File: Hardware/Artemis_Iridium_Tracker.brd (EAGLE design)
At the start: 50.8 x 50.8 mm, 160 parts, among them J1 IRIDIUM_9603N, J14 CORTEX_DEBUG, J3 PTH, J8 uFL, J9 SMA-142-0711-821/826, Q1 DMG3414U-7, Q2 DMG3415U-7, U10 MCP73831, U2 LTC3225EDDB#TRMPBF, U3 ADM4210-1, U4 UBLOX_ZOE_M8-0-10, U5 AS179-92LF, U6 MS8607-02BA01, U7 ARTEMIS_MODULESMD, U8 AP3429A, U9 CH340E, Y1 32.768kHz, Y2 32.768kHz

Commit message: Updated the PCB - still work in progress!
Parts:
- removed BYP: (no value), SparkFun-Jumpers:SMT-JUMPER_2_NO_SILK
- removed C32: 0.1uF, SparkFun-Capacitors:0603
- removed C33: 1nF, SparkFun-Capacitors:0603
- removed C34, C35: 4.7uF, SparkFun-Capacitors:0603
- removed D15: 3A/10V/280mV, SparkFun-DiscreteSemi:SOD-323
- removed F1: 6V/2A, SparkFun-Fuses:1210
- removed J10: (no value), SparkFun-Connectors:USB-C-16P
- removed J11: (no value), SparkFun-Connectors:1X05
- removed J12: (no value), SparkFun-Connectors:JST-2-SMD
- removed J14: CORTEX_DEBUG, SparkFun-Connectors:2X5-PTH-1.27MM-NO_SILK
- removed J16: (no value), SparkFun-Connectors:JST04_1MM_RA
- removed J8: uFL, microbuilder:U.FL
- removed J9: SMA-142-0711-821/826, con-coax:J502-ND-142-0711-821/826
- removed JP3: JUMPER-SMT_2_NC_TRACE_SILK, SparkFun-Jumpers:SMT-JUMPER_2_NC_TRACE_SILK
- removed L3: 2.2μH, SparkFun-Coils:INDUCTOR_4X4MM
- removed LOGO1: OSHW-LOGOMINI, SparkFun-Aesthetics:OSHW-LOGO-MINI
- removed LOGO2: SFE_LOGO_NAME.1_INCH, SparkFun-Aesthetics:SFE_LOGO_NAME_.1
- removed LOGO3: SFE_LOGO_NAME_FLAME.1_INCH, SparkFun-Aesthetics:SFE_LOGO_NAME_FLAME_.1
- removed S2: RESET, SparkFun-Switches:TACTILE_SWITCH_SMD_5.2MM
- removed U10: MCP73831, SparkFun-IC-Power:SOT23-5
- removed Y1, Y2: 32.768kHz, SparkFun-Clocks:CRYSTAL-SMD-3.2X1.5MM
- added !RESET, EN, GND: (no value), SparkFun-Connectors:1X01_NO_SILK
- added 3V3EN: (no value), SparkFun-Jumpers:SMT-JUMPER_2_NC_TRACE_SILK
- added 5V3, BUSV, RX(OUT), RX0, TX(IN), TX0: TEST-POINT3X5, SparkFun-Connectors:PAD.03X.05
- added C1: 10nF, SparkFun-Capacitors:0603
- added C7: 0.1uF, SparkFun-Capacitors:0603
- added C8: 4.7uF, SparkFun-Capacitors:0603
- added D13: Yellow, SparkFun-LED:LED-0603
- added DEBUG: CORTEX_DEBUG, SparkFun-Connectors:2X5-PTH-1.27MM-NO_SILK
- added I2C: PTH, SparkX:1X04_NO_SILK
- added JP2: JUMPER-SMT_2_NC_TRACE_SILK, SparkFun-Jumpers:SMT-JUMPER_2_NC_TRACE_SILK
- added L2: 2.2μH, SparkFun-Coils:INDUCTOR_4X4MM
- added LOGO4: OSHW-LOGOMINI, SparkFun-Aesthetics:OSHW-LOGO-MINI
- added Q3: DMG3415U-7, microbuilder:SOT23-WIDE
- added Q4: 2N2222, transistor:SOT23-BEC
- added QWIIC: (no value), SparkFun-Connectors:JST04_1MM_RA
- added R2, R3: 1k, SparkFun-Resistors:0603
- added R20, R4: 5.1k, SparkFun-Resistors:0603
- added R30: 10k, SparkFun-Resistors:0603
- added S1: RESET, SparkFun-Switches:TACTILE_SWITCH_SMD_5.2MM
- added SPI: (no value), SparkFun-Connectors:1X07
- added U$29, U$30: SPARKX-LOGO4, SparkX:SPARKX-MEDIUM
- added U$31: (no value), SCK_BOT:SCK0
- added U$32: (no value), 5.3V:5#3V0
- added U$33: (no value), RX:RX0
- added U$34: (no value), RX0:RX00
- added U$35: (no value), RX1:RX10
- added U$36: (no value), SAFEBOOT:SAFEBOOT0
- added U$37: (no value), TX:TX0
- added U$38: (no value), TX0:TX00
- added U$39: (no value), TX1:TX10
- added U$40: (no value), ARTEMIS:ARTEMIS0
- added U$41: (no value), IRIDIUM:IRIDIUM0
- added U$42: (no value), TRACKER:TRACKER0
- added U$43: (no value), PWR_LED:PWR_LED0
- added U$44: (no value), VBUS:VBUS0
- added U$45: (no value), GND:GND0
- added U$46: (no value), EN:EN0
- added U$47: (no value), 3.3V EN:3#3V_EN0
- added U$48: (no value), MEAS:MEAS0
- added U$49: (no value), LiPo:LIPO0
- added U1: CH340E_MSOP10, SparkFun-IC-Comms:MSOP10
- added X1, X2: 32.768kHz, SparkFun-Clocks:CRYSTAL-SMD-3.2X1.5MM
- BAT1, BAT2, BAT3: device SparkFun-Electromechanical:BATTERY-AAA-KEYSTONE92 -> Iridium_9603_Beacon:BATTERY-AAA-KEYSTONE82
- C17: value 1.0uF -> 4.7uF
- C29: value 10nF -> 1nF
- D7: value Yellow -> GREEN
- D8: value GREEN -> 3A/10V/280mV; device SparkFun-LED:LED-0603 -> SparkFun-DiscreteSemi:SOD-323
- J2: value (none) -> USB-C; device SparkFun-Connectors:1X02_NO_SILK -> SparkFun-Connectors:USB-C-16P
- J3: value PTH -> (none); device SparkX:1X04_NO_SILK -> SparkFun-Connectors:JST-2-SMD
- J5: device SparkFun-Connectors:1X01_NO_SILK -> SparkFun-Connectors:JST-2-SMD
- J6: value (none) -> uFL; device SparkFun-Connectors:1X01_NO_SILK -> microbuilder:U.FL
- J7: value (none) -> SMA-142-0711-821/826; device SparkFun-Connectors:1X01_NO_SILK -> con-coax:J502-ND-142-0711-821/826
- R22: value 1k -> 10k
- R23: value 330 -> 10k; device SparkFun-Resistors:0603@2 -> SparkFun-Resistors:0603
- R24: value 5.1k -> 20k; device SparkFun-Resistors:0603@2 -> SparkFun-Resistors:0603
- R25: value 5.1k -> 1k; device SparkFun-Resistors:0603@2 -> SparkFun-Resistors:0603
- U$11: device 5.3V_OUT:5#3V0 -> MISO:MISO0
- U$12, U$17: device Qwiic_007:QWIIC0 -> Labels-0_04:GND1
- U$16, U$7: device Labels:RST#-[> -> RESET:#RESET0
- U$18: device Iridium_007:IRIDIUM0 -> SCK:SCK0
- U$19: device Iridium_007:IRIDIUM0 -> GNSS:GNSS0
- U$20, U$24: device 9603N_007:9603N0 -> Labels-0_04:3#3V2
- U$25: device Qwiic_Bubble:QWIIC0 -> MOSI_BOT:MOSI0
- U$28: device 5.3V_OUT:5#3V0 -> MISO_BOT:MISO0
- U$5: device Labels-0_04:SDA8 -> SCL_BOT:SCL0
- U$6: device Labels-0_04:SCL9 -> SDA_BOT:SDA0
- U$8: device Labels:I_SUPER2_C-()-03 -> MOSI:MOSI0
- U9: value CH340E -> MCP73831; device SparkFun-IC-Comms:MSOP10 -> SparkFun-IC-Power:SOT23-5
- moved D14 158.9 mm to (11.4, 38.1), turned to 180 degrees
- moved BAT1 158.8 mm to (5.08, 38.1), turned to 270 degrees
- moved D10 158.2 mm to (11.4, 40.6), turned to 180 degrees
- moved BAT2 133.6 mm to (31.8, 5.08)
- moved U6 133.2 mm to (8.89, 31.1), turned to 180 degrees
- moved C12 131.4 mm to (11.8, 30.9), turned to 90 degrees
- moved GPS_RX 129.8 mm to (48.3, 50.8)
- moved GPS_TX 129.8 mm to (48.3, 48.3)
- moved SAFEBOOT 125.6 mm to (50.8, 55.9)
- moved D9 115.6 mm to (10.3, 15.2)
- moved U$15 112.1 mm to (11.3, 62.6), flipped to the bottom
- moved R29 111.7 mm to (10.3, 17.4)
- moved R28 110.5 mm to (7.62, 20.7), turned to 90 degrees
- moved D1 110.2 mm to (52.8, 18.0)
- moved D2 110.2 mm to (52.8, 20.5)
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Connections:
- removed net ARTEMIS_SHLD: J10.SHLD1, J10.SHLD2, J10.SHLD3, J10.SHLD4, J10.SHLD5, J10.SHLD6, J10.SHLD7, J10.SHLD8
- removed net CC1: J10.A5, R25.2
- removed net CC2: J10.B5, R24.2
- removed net D+1: J10.A6, J10.B6, U9.1
- removed net D-1: J10.A7, J10.B7, U9.2
- removed net N$38 (its old number): BYP.1, F1.1, J10.VBUS1, J10.VBUS2
- new net CC3: J2.B5, R4.2
- new net CC4: J2.A5, R20.2
- new net D+2: J2.A6, J2.B6, U1.1
- new net D-2: J2.A7, J2.B7, U1.2
- new net N$22: D7.A, R3.1
- new net N$34: D13.A, R2.1
- new net N$46: Q3.3, R24.1
- new net N$47: Q4.B, R25.2
- new net SHLD: J2.SHLD1, J2.SHLD2, J2.SHLD3, J2.SHLD4, J2.SHLD5, J2.SHLD6, J2.SHLD7, J2.SHLD8
- net 3.3V: now also C1.1, C12.1, C7.1, DEBUG.1, I2C.2, JP2.2, L2.P$2, QWIIC.2, R2.2, R3.2, SPI.7, U1.10, U1.7, U6.1; no longer C17.1, C29.1, C30.1, J11.5, J14.1, J16.2, L3.P$2, R1.2, R22.2, R23.2, U9.10, U9.7
- net 3V3SW: no longer C12.1, J3.2, U6.1
- net ANTENNA: now also J7.1; no longer J9.1
- net ARTEMIS_!RESET: now also !RESET.1, C29.1, DEBUG.10, S1.3, S1.4; no longer C33.1, J14.10, J5.1, S2.3, S2.4
- net ARTEMIS_!RTS!: now also C30.1, U1.4; no longer C32.1, U9.4
- net ARTEMIS_BOOT: now also C30.2; no longer C32.2
- net ARTEMIS_D10: now also U4.50; no longer U4.36
- net ARTEMIS_D13: now also BUSV.P$1, R23.1, R24.2
- net ARTEMIS_D24: now also TX(IN).P$1
- net ARTEMIS_D25: now also RX(OUT).P$1
- net ARTEMIS_D33: now also DEBUG.6; no longer J14.6
- net ARTEMIS_D34: now also R25.1, R30.1
- net ARTEMIS_D35: now also SPI.5
- net ARTEMIS_D39_SCL4: now also QWIIC.4; no longer J16.4
- net ARTEMIS_D4: now also SPI.6
- net ARTEMIS_D40_SDA4: now also QWIIC.3; no longer J16.3
- net ARTEMIS_D42: no longer J6.1
- net ARTEMIS_D5_SCK: now also SPI.4; no longer J11.4
- net ARTEMIS_D6_MISO: now also SPI.3; no longer J11.3
- net ARTEMIS_D7_MOSI: now also SPI.2; no longer J11.2
- net ARTEMIS_D8_SCL: now also I2C.4; no longer J3.4
- net ARTEMIS_D9_SDA: now also I2C.3; no longer J3.3
- net ARTEMIS_RX0: now also D13.C, RX0.P$1, U1.8; no longer D7.C, U9.8
- net ARTEMIS_SWDCK: now also DEBUG.4; no longer J14.4
- net ARTEMIS_SWDIO: now also DEBUG.2; no longer J14.2
- net ARTEMIS_TX0: now also D7.C, TX0.P$1, U1.9; no longer D8.C, U9.9
- net EXT_PWR: now also 5V3.P$1; no longer J7.1
- net GND: now also C1.2, C7.2, C8.2, DEBUG.3, DEBUG.5, DEBUG.9, GND.1, I2C.1, J2.GND, J2.GND2, J5.1, J6.1, J6.2, J7.G@1, J7.G@2, J7.G@3, J7.G@4, Q4.E, QWIIC.1, R20.1, R23.2, R30.2, R4.1, S1.1, S1.2, SPI.1, U1.3, U9.2; no longer C30.2, C33.2, C34.2, C35.2, J10.GND, J10.GND2, J11.1, J12.1, J14.3, J14.5, J14.9, J16.1, J2.1, J8.1, J8.2, J9.G@1, J9.G@2, J9.G@3, J9.G@4, R24.1, R25.1, S2.1, S2.2, U10.2, U9.3
- net IRIDIUM: now also J6.3; no longer J8.3
- net N$18: now also X2.P$2; no longer Y1.P$2
- net N$19: now also X2.P$1; no longer Y1.P$1
- net N$23: now also D1.A; no longer JP3.2
- net N$3: now also JP2.1, R1.2; no longer D1.A, JP3.1
- net N$31: now also X1.P$1; no longer Y2.P$1
- net N$33: now also L2.P$1; no longer L3.P$1
- net N$36: now also 3V3EN.2, EN.1, U8.1; no longer D8.A, R23.1
- net N$37: now also Q3.1, Q4.C; no longer D7.A
- net N$39: now also U9.5; no longer U10.5
- net N$41: now also U9.1; no longer U10.1
- net N$42: now also J3.2
- net N$45: now also D8.C; no longer D15.C
- net N$7: now also X1.P$2; no longer Y2.P$2
- net VIN: now also 3V3EN.1, Q3.2, R22.2; no longer U8.1
- net V_BATT: now also C8.1, D8.A, J5.2, U9.3; no longer C35.1, D15.A, J12.2, J2.2, U10.3
- net V_USB: now also C17.1, J2.VBUS1, J2.VBUS2, U9.4; no longer BYP.2, C34.1, F1.2, U10.4
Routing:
- net GND: track 54.0 -> 185.8 mm, vias 11 -> 45
- net N$42: track 0.00 -> 115.9 mm, vias 0 -> 2
- net V_USB: track 0.00 -> 64.3 mm, vias 0 -> 2
- net N$24: track 0.00 -> 53.7 mm, vias 0 -> 2
- net 3.3V: track 0.00 -> 44.1 mm, vias 0 -> 1
- net V_BATT: track 0.00 -> 39.0 mm, vias 0 -> 2
- net ARTEMIS_BOOT: track 0.00 -> 31.6 mm, vias 0 -> 4
- net N$43: track 0.00 -> 30.8 mm
- net N$38: track 0.00 -> 30.8 mm
- net N$1: track 18.2 -> 45.4 mm, vias 0 -> 1
- net LTC3225_VOUT: track 22.1 -> 48.6 mm
- net ARTEMIS_!RESET: track 0.00 -> 25.3 mm
- net VIN: track 0.00 -> 24.4 mm, vias 0 -> 1
- net ARTEMIS_D9_SDA: track 0.00 -> 16.9 mm, vias 0 -> 1
- net ARTEMIS_D8_SCL: track 0.00 -> 16.2 mm, vias 0 -> 1
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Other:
- board size 50.8 x 50.8 mm -> 63.5 x 69.8 mm
- board text added: "To Do: Check the height clearance for L2"
- board text removed: "RX"
- board text removed: "TX"

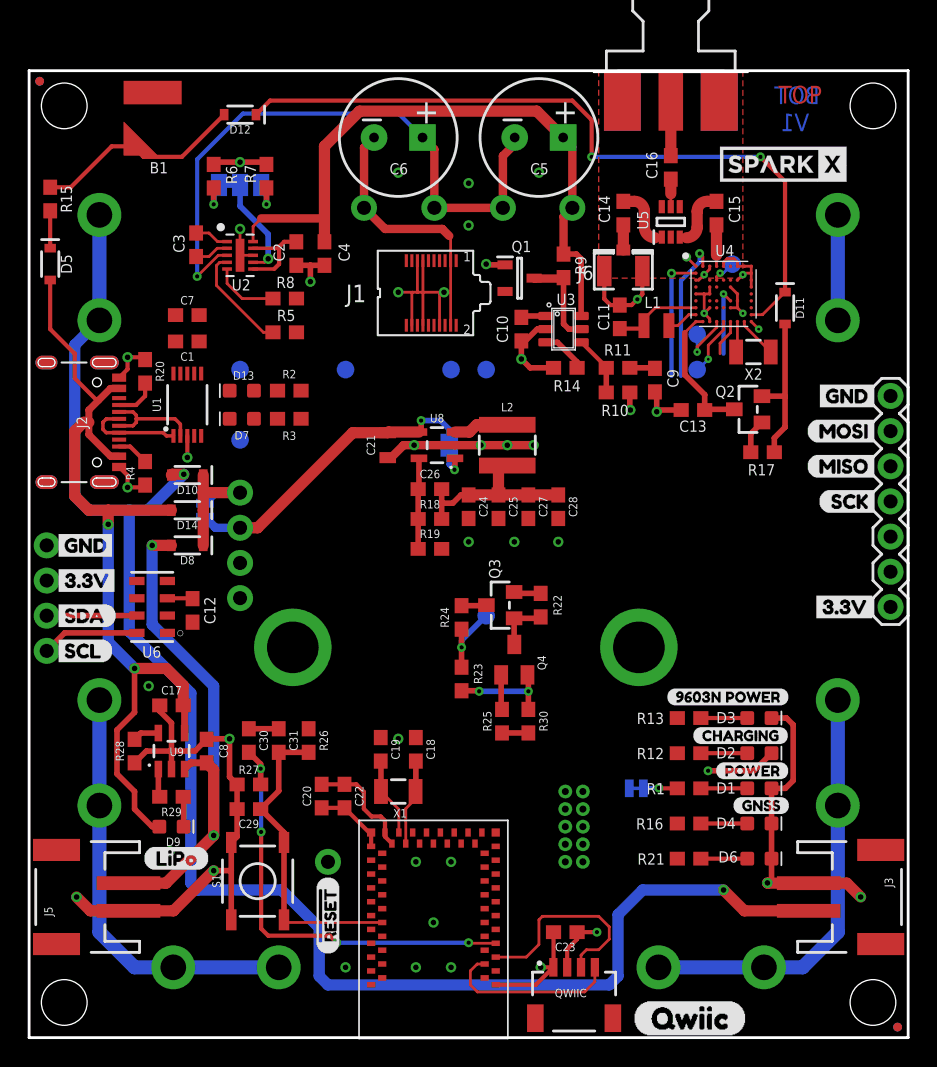
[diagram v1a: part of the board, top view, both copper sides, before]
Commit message: PCB is routed - grounding needs checking
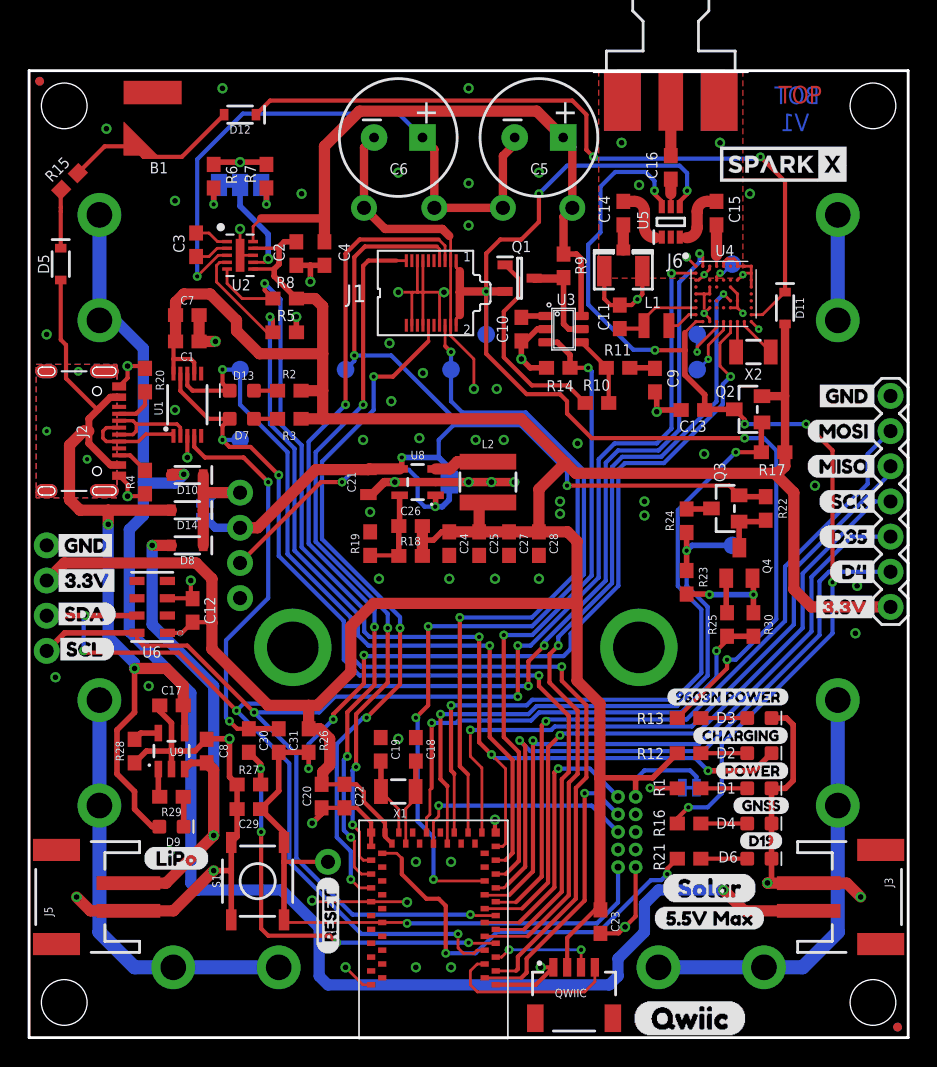
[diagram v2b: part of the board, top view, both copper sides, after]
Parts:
- added U$50: (no value), D19:D190
- added U$51: (no value), D4:D40
- added U$52: (no value), D4_BOT:D40
- added U$54: (no value), D35:D350
- added U$55: (no value), D35_BOT:D350
- added U$56: (no value), VBUS_3:VBUS#30
- added U$57: (no value), Solar:SOLAR0
- added U$58: (no value), 5V5 Max:5#5V_MAX0
- moved BUSV 18.5 mm to (50.8, 35.6)
- moved Q3 17.7 mm to (50.3, 38.2)
- moved Q4 17.7 mm to (51.3, 34.3)
- moved R22 17.7 mm to (53.2, 38.2)
- moved R25 17.7 mm to (50.4, 29.8)
- moved R30 17.7 mm to (52.3, 29.8)
- moved R23 17.7 mm to (47.5, 32.9)
- moved R24 17.7 mm to (47.5, 37.3)
- moved U$43 14.9 mm to (52.3, 20.2), turned to 0 degrees
- moved R19 4.33 mm to (24.6, 35.7), turned to 270 degrees
- moved JP2 3.84 mm to (47.7, 18.1), turned to 180 degrees
- moved DEBUG 3.83 mm to (43.2, 14.9), turned to 270 degrees
- moved C21 3.01 mm to (24.5, 40.1)
- moved C24 3.01 mm to (30.4, 35.7)
- moved C25 3.01 mm to (32.5, 35.7)
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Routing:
- net 3.3V: track 44.1 -> 246.5 mm, vias 1 -> 0
- net ARTEMIS_D9_SDA: track 16.9 -> 112.9 mm, vias 1 -> 7
- net ARTEMIS_D8_SCL: track 16.2 -> 104.9 mm, vias 1 -> 5
- net EXT_PWR: track 0.00 -> 86.8 mm, vias 0 -> 5
- net ARTEMIS_!RESET: track 25.3 -> 103.0 mm, vias 0 -> 5
- net ARTEMIS_RX0: track 0.00 -> 72.9 mm, vias 0 -> 2
- net ARTEMIS_D28: track 9.92 -> 80.5 mm, vias 1 -> 4
- net ARTEMIS_D25: track 0.00 -> 68.2 mm, vias 0 -> 2
- net ARTEMIS_TX0: track 0.00 -> 66.2 mm, vias 0 -> 3
- net 3V3SW: track 9.97 -> 74.8 mm, vias 0 -> 6
- net ARTEMIS_D24: track 0.00 -> 60.6 mm, vias 0 -> 4
- net ARTEMIS_D17: track 0.00 -> 58.9 mm, vias 0 -> 4
- net ARTEMIS_D10: track 5.03 -> 59.4 mm, vias 1 -> 2
- net ARTEMIS_D27: track 7.78 -> 61.4 mm, vias 0 -> 2
- net ARTEMIS_D7_MOSI: track 0.00 -> 52.6 mm, vias 0 -> 1
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- added copper zone on layer 1, net SHLD
- added copper zone on layer 16, net SHLD
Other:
- board text removed: "To Do: Check the height clearance for L2"

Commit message: Final PCB tweaks - ready for prototyping!
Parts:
- added U10: MCP111T-240E/TT, Microchip-MCP11:SOT95P237X112-3N
- moved D5 6.23 mm to (8.51, 55.5)
- moved R15 5.95 mm to (8.51, 59.8), turned to 270 degrees
- moved U$36 0.85 mm to (55.5, 57.7)
- moved C12 0.51 mm to (11.8, 30.4)
- moved U$33 0.51 mm to (47.5, 50.8)
- moved U$37 0.51 mm to (47.5, 48.3)
- moved MEAS 0.38 mm to (12.3, 38.1)
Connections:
- net 3.3V: now also U10.3
- net ARTEMIS_!RESET: now also U10.1
- net GND: now also U10.2
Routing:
- net GND: track 212.3 -> 292.4 mm, vias 84 -> 103
- net ARTEMIS_!RTS!: track 29.6 -> 41.8 mm
- net V_USB: track 64.7 -> 68.0 mm
- net ARTEMIS_D41: track 50.6 -> 53.7 mm
- net ARTEMIS_D17: track 58.9 -> 61.8 mm
- net ARTEMIS_D18: track 51.7 -> 54.3 mm
- net N$20: track 4.23 -> 2.32 mm
- net V_BCKP: track 12.9 -> 11.1 mm
- net ARTEMIS_D8_SCL: track 104.9 -> 103.2 mm
- net ARTEMIS_RX0: track 72.9 -> 71.2 mm
- net 3V3SW: track 74.8 -> 76.3 mm
- net ARTEMIS_D24: track 60.6 -> 59.2 mm
- net 3.3V: track 246.5 -> 247.8 mm
- net ARTEMIS_!RESET: track 103.0 -> 104.3 mm, vias 5 -> 7
- net ARTEMIS_TX0: track 66.2 -> 65.1 mm
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
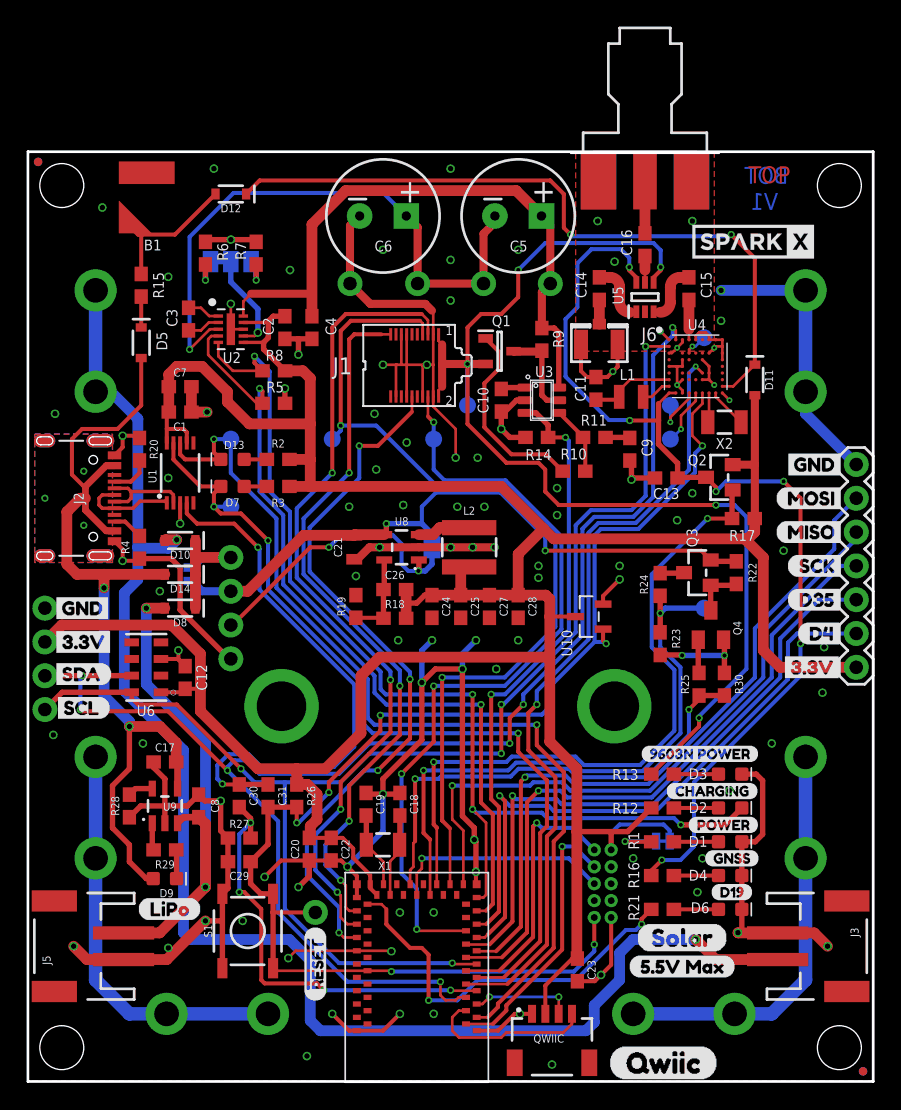
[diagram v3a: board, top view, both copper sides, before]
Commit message: Tweaked the SMA position
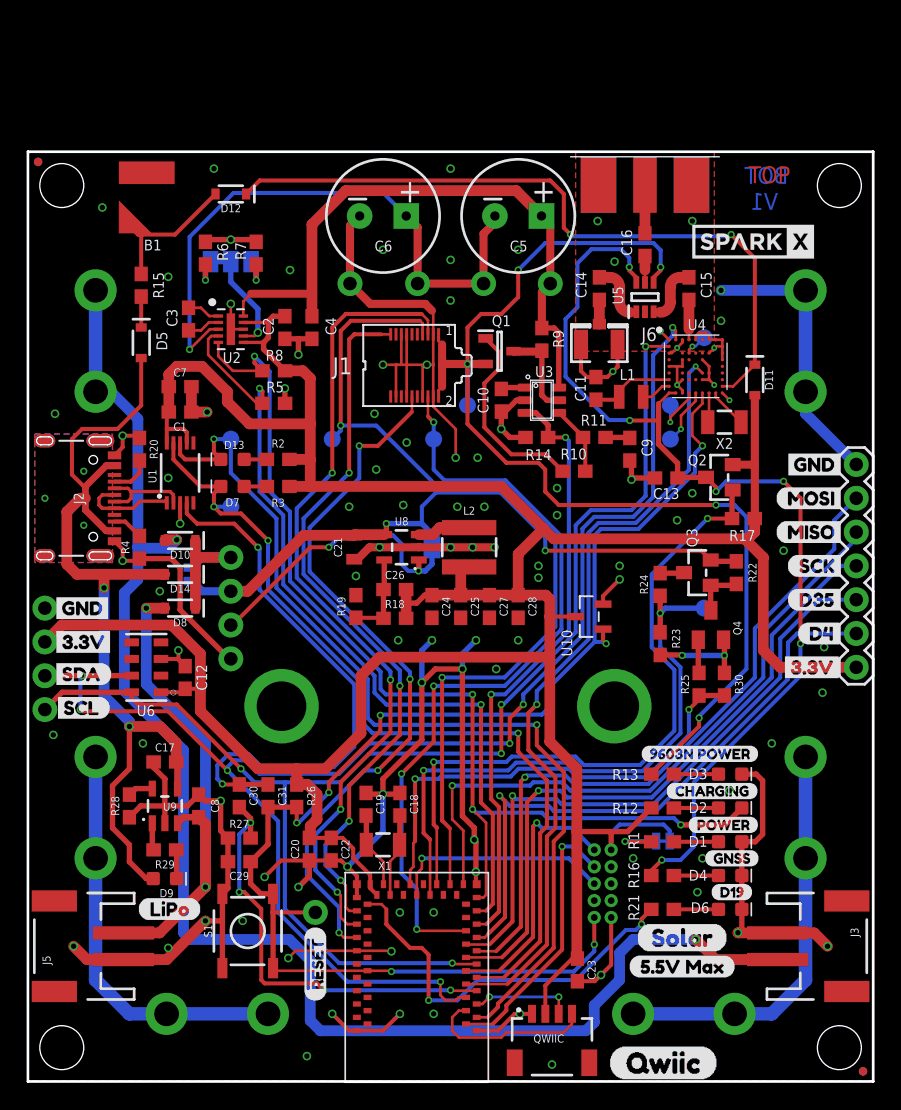
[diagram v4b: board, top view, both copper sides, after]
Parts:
- J7: value SMA-142-0711-821/826 -> SMA-; device con-coax:J502-ND-142-0711-821/826 -> Qwiic_Iridium_9603N:J502-ND-142-0711-821/826_NO_CREAM
- moved J7 0.25 mm to (46.4, 69.5)

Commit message: Substantial update for V2 (X01) of the PCB
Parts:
- removed BAT1, BAT2, BAT3: (no value), Iridium_9603_Beacon:BATTERY-AAA-KEYSTONE82
- removed BUSV: TEST-POINT3X5, SparkFun-Connectors:PAD.03X.05
- removed C26: 22pF, SparkFun-Capacitors:0603
- removed L2: 2.2μH, SparkFun-Coils:INDUCTOR_4X4MM
- removed R18: 453k, SparkFun-Resistors:0603@2
- removed R19: 100k, SparkFun-Resistors:0603@2
- removed U$45: (no value), GND:GND0
- removed U$46: (no value), EN:EN0
- removed U$56: (no value), VBUS_3:VBUS#30
- removed U8: AP3429A, SparkFun-IC-Power:SOT23-5@1
- added U$59: (no value), GND:GND0
- added U$60: (no value), VIN:VIN0
- added U$61: (no value), 3xAA:3_X_AA0
- added U$62: (no value), 3xAAA:3_X_AAA0
- added U$63: (no value), 6VMax:6V_MAX0
- added U$64: (no value), Solar:SOLAR0
- added U$65: (no value), VINdiv3:VIN#30
- added U$66: (no value), Qwiic:QWIIC0
- added U11: 3.3V, SparkFun-IC-Power:SOT23-5
- added VIN/3: TEST-POINT3X5, SparkFun-Connectors:PAD.03X.05
- C24: value 22uF -> 1.0uF
- D10, D11, D12, D14, D8: value 3A/10V/280mV -> 0.5A/40V/420mV
- J7: value SMA- -> ANTENNA-GROUNDEDEDGE_SMA; device Qwiic_Iridium_9603N:J502-ND-142-0711-821/826_NO_CREAM -> Qwiic_Iridium_9603N:SMA-EDGE
- U$16: device RESET:#RESET0 -> TX0:TX00
- U$23: device Qwiic_Bubble:QWIIC0 -> RX0:RX00
- U$57: device Solar:SOLAR0 -> LiPo:LIPO0
- U$58: device 5V5 Max:5#5V_MAX0 -> EN:EN0
- U$7: device RESET:#RESET0 -> RST:#RST0
- moved JP9 82.6 mm to (2.54, 61.0)
- moved JP10 74.2 mm to (48.3, 61.0)
- moved JP12 66.0 mm to (48.3, 2.54)
- moved JP11 64.8 mm to (2.54, 2.54)
- moved B1 57.7 mm to (37.0, 15.6)
- moved R15 55.8 mm to (36.6, 11.6), turned to 180 degrees
- moved U$30 52.3 mm to (3.20, 52.7), turned to 90 degrees
- moved D5 50.1 mm to (32.6, 11.6), turned to 180 degrees
- moved U$58 43.6 mm to (2.03, 15.2)
- moved D12 42.6 mm to (42.0, 33.5), turned to 270 degrees
- moved U$23 39.4 mm to (7.87, 18.0), turned to 90 degrees
- moved R20 38.7 mm to (8.64, 8.76), turned to 0 degrees
- moved J2 37.6 mm to (10.8, 6.48), turned to 0 degrees
- moved 3V3EN 37.2 mm to (3.81, 14.1), turned to 90 degrees
- moved R2 35.6 mm to (7.87, 12.8), turned to 90 degrees
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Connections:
- net N$45 renamed VBUS
- removed net ARTEMIS_D0: U7.D0
- removed net ARTEMIS_D1: U7.D1
- removed net ARTEMIS_D11: U7.~AD11
- removed net ARTEMIS_D12: U7.~AD12
- removed net ARTEMIS_D14_TX1: U7.D14
- removed net ARTEMIS_D15_RX1: U7.D15
- removed net ARTEMIS_D16: U7.AD16
- removed net ARTEMIS_D2: U7.D2
- removed net ARTEMIS_D23: U7.~D23
- removed net ARTEMIS_D29: U7.~AD29
- removed net ARTEMIS_D3: U7.D3
- removed net ARTEMIS_D31: U7.~AD31
- removed net ARTEMIS_D32: U7.~AD32
- removed net ARTEMIS_D36_PDMDATA: U7.D36
- removed net ARTEMIS_D37_PDMCLK: U7.~D37
- removed net ARTEMIS_D38: U7.D38
- removed net ARTEMIS_D42: U7.~D42
- removed net ARTEMIS_D43: U7.~D43
- removed net ARTEMIS_D44: U7.~D44
- removed net ARTEMIS_D45: U7.~D45
- removed net N$33: L2.P$1, U8.3
- removed net N$34: D13.A, R2.1
- removed net N$38: BAT1.GND@1, BAT1.GND@2, BAT2.PWR@1, BAT2.PWR@2
- removed net N$42: BAT1.PWR@1, BAT1.PWR@2, D10.A, J3.2
- removed net N$43: BAT2.GND@1, BAT2.GND@2, BAT3.PWR@1, BAT3.PWR@2
- new net V_AAA: D10.A, J3.2
- net 3.3V: now also D13.A, D7.A, R1.2, U11.5; no longer C26.1, JP2.2, L2.P$2, R18.2, R2.2, R3.2
- net ANTENNA: now also J7.SIG; no longer J7.1
- net ARTEMIS_D13: now also VIN/3.P$1; no longer BUSV.P$1
- net ARTEMIS_RX0: now also R2.1; no longer D13.C
- net ARTEMIS_TX0: now also R3.1; no longer D7.C
- net GND: now also J7.GND@0, J7.GND@1, J7.GND@2, J7.GND@3, U11.2; no longer BAT3.GND@1, BAT3.GND@2, J7.G@1, J7.G@2, J7.G@3, J7.G@4, R19.1, U8.2
- net N$22: now also D13.C, R2.2; no longer D7.A, R3.1
- net N$23: now also JP2.1; no longer R1.1
- net N$3: now also JP2.2, R1.1; no longer JP2.1, R1.2
- net N$32: now also D7.C, R3.2; no longer C26.2, R18.1, R19.2, U8.5
- net N$36: now also U11.3; no longer U8.1
- net VIN: now also U11.1; no longer U8.4
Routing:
- net N$42: track 112.4 -> 0.00 mm, vias 2 -> 0
- net 3.3V: track 247.8 -> 196.1 mm, vias 0 -> 2
- net ARTEMIS_D25: track 67.9 -> 28.6 mm
- net N$24: track 53.8 -> 19.0 mm
- net V_BATT: track 39.0 -> 8.15 mm, vias 2 -> 0
- net N$43: track 30.8 -> 0.00 mm
- net N$38: track 30.8 -> 0.00 mm
- net ARTEMIS_RX0: track 71.2 -> 41.1 mm
- net ARTEMIS_D13: track 46.4 -> 17.5 mm, vias 2 -> 3
- net ARTEMIS_D26: track 51.3 -> 23.8 mm
- net VBUS: track 11.0 -> 38.0 mm, vias 0 -> 4
- net ARTEMIS_D24: track 59.2 -> 32.4 mm, vias 4 -> 2
- net ARTEMIS_D17: track 61.8 -> 35.2 mm, vias 4 -> 2
- net VIN: track 49.7 -> 76.0 mm, vias 2 -> 3
- net ARTEMIS_D41: track 53.7 -> 28.2 mm, vias 4 -> 2
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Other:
- board size 63.5 x 69.8 mm -> 50.8 x 63.5 mm
- board text added: "X01"
- board text removed: "V1"
